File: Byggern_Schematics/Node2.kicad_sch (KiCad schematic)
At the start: 0 parts

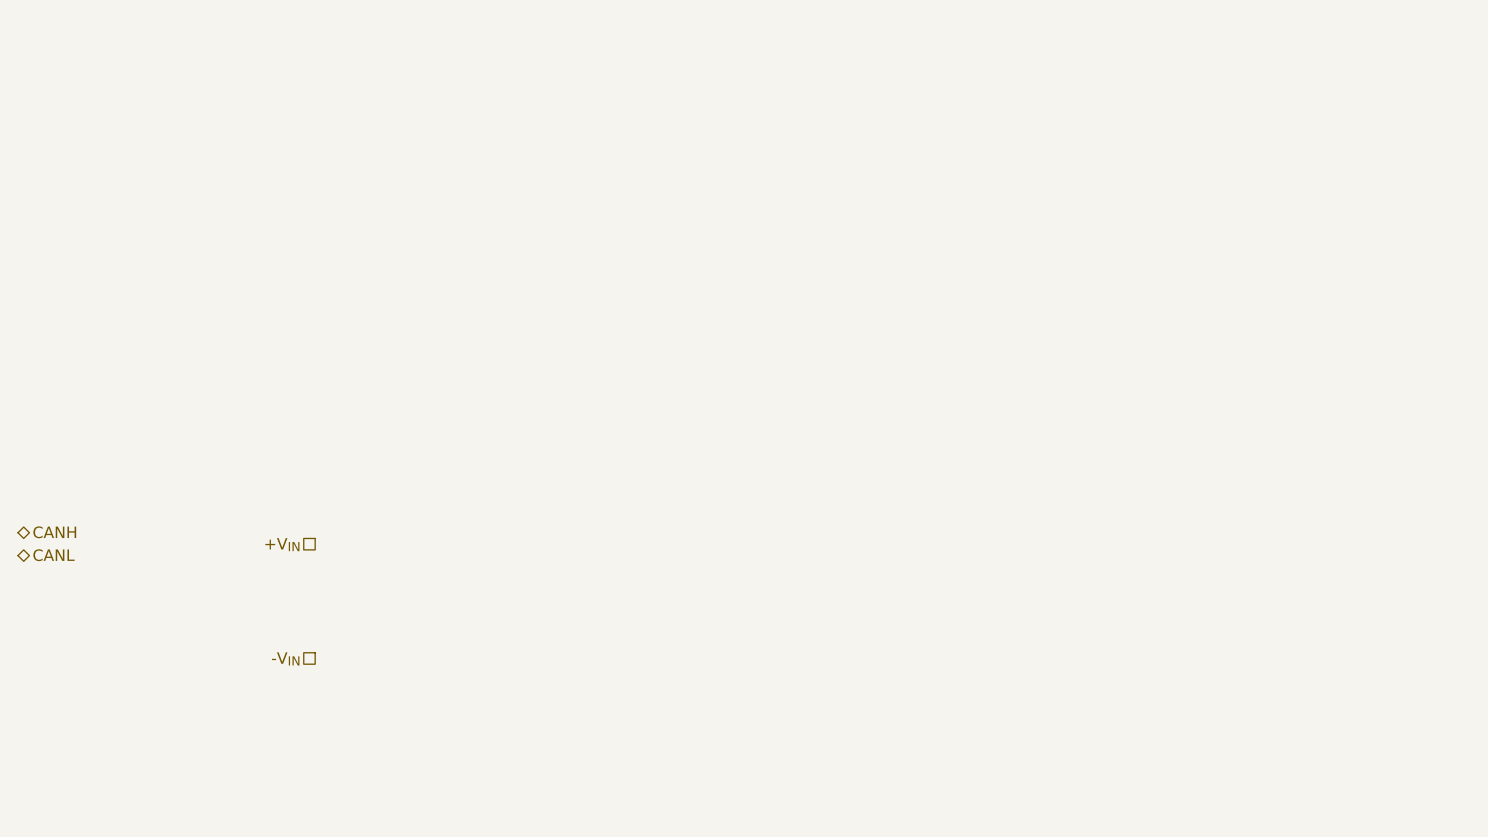
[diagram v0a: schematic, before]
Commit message: A lot of schematic changes
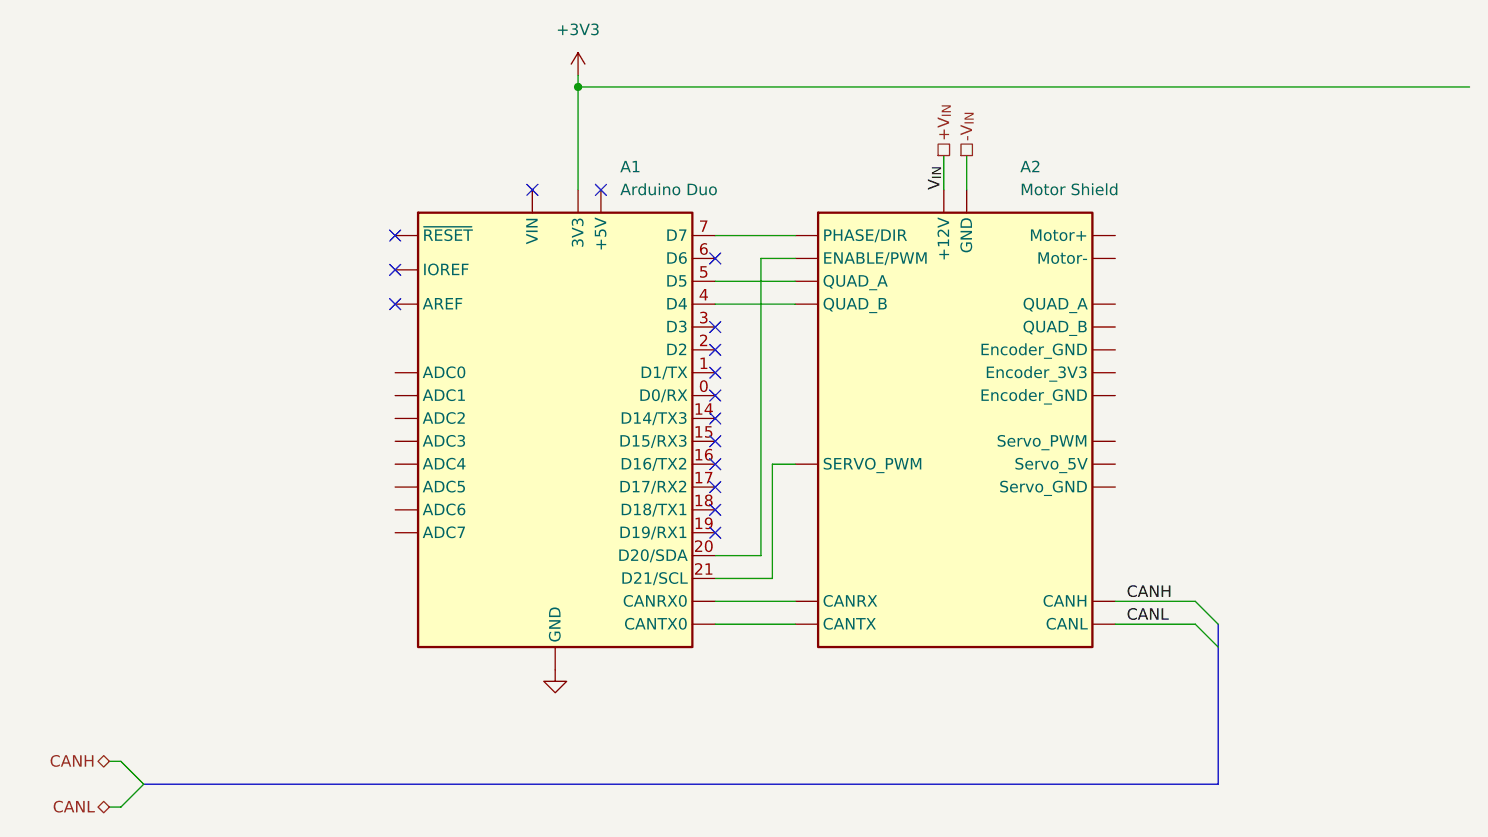
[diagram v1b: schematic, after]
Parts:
- added A1: Arduino Duo, Module:Arduino_UNO_R3, symbol MCU_Module:Arduino_UNO_R3
- added A2: Motor Shield, Module:Arduino_UNO_R3, symbol MCU_Module:Arduino_UNO_R3
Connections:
- net +V_{IN}: now also A2. (CANL)
- net -V_{IN}: now also A2. (CANL)
- net CANH: now also A2. (CANL)
- net CANL: now also A2. (CANL)
- new net: A1. (CANTX0), A2. (CANL) (x2)
- new net: A1.20 (D20/SDA), A2. (CANL)
- new net: A1.21 (D21/SCL), A2. (CANL)
- new net: A1.4 (D4), A2. (CANL)
- new net: A1.5 (D5), A2. (CANL)
- new net: A1.7 (D7), A2. (CANL)
- new net +3V3: A1. (CANTX0)
- new net GND: A1. (CANTX0)
- no-connect marks 0 -> 16
